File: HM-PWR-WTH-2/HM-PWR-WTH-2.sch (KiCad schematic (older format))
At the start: 42 parts, among them J101 Screw_Terminal_01x02, J102 Conn_01x02_Male, J103 Conn_01x02_Male, J104 Conn_01x02_Male, J105 Conn_01x02_Male, J106 USB_B_Micro, SW101 SW_Push, SW102 SW_Push, U101 LT8606xMSE

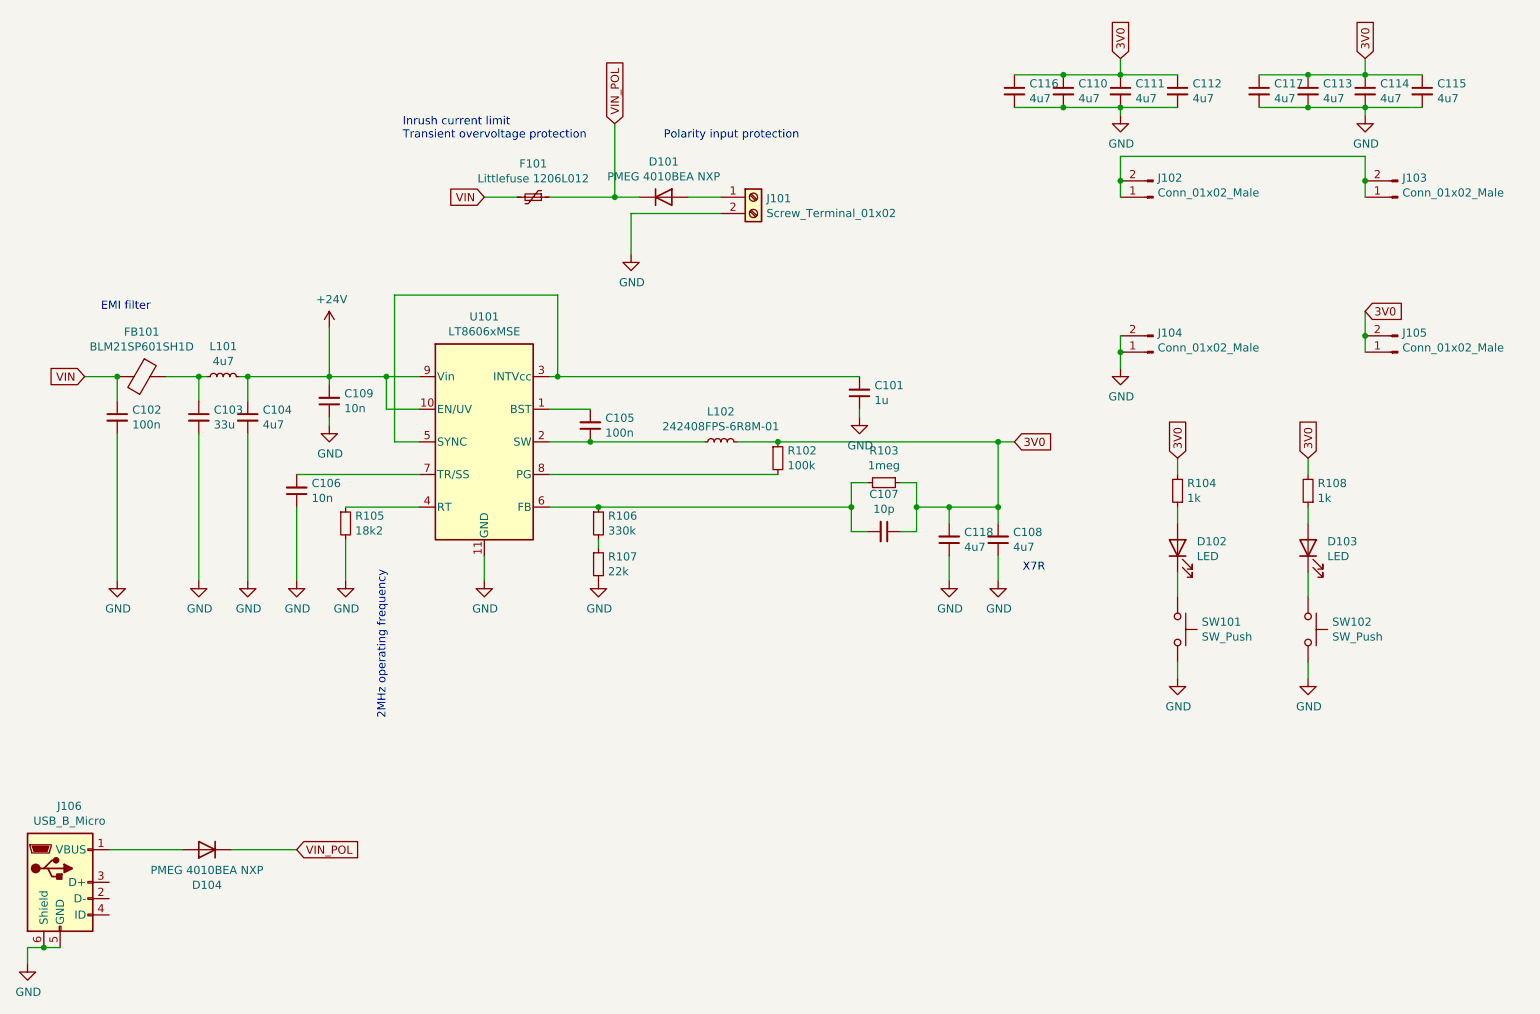
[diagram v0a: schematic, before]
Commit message: HM-PWR-WTH-2: Switch to TPS70930
Signed-off-by: Patrick Rudolph <patrick.rudolph@9elements.com>
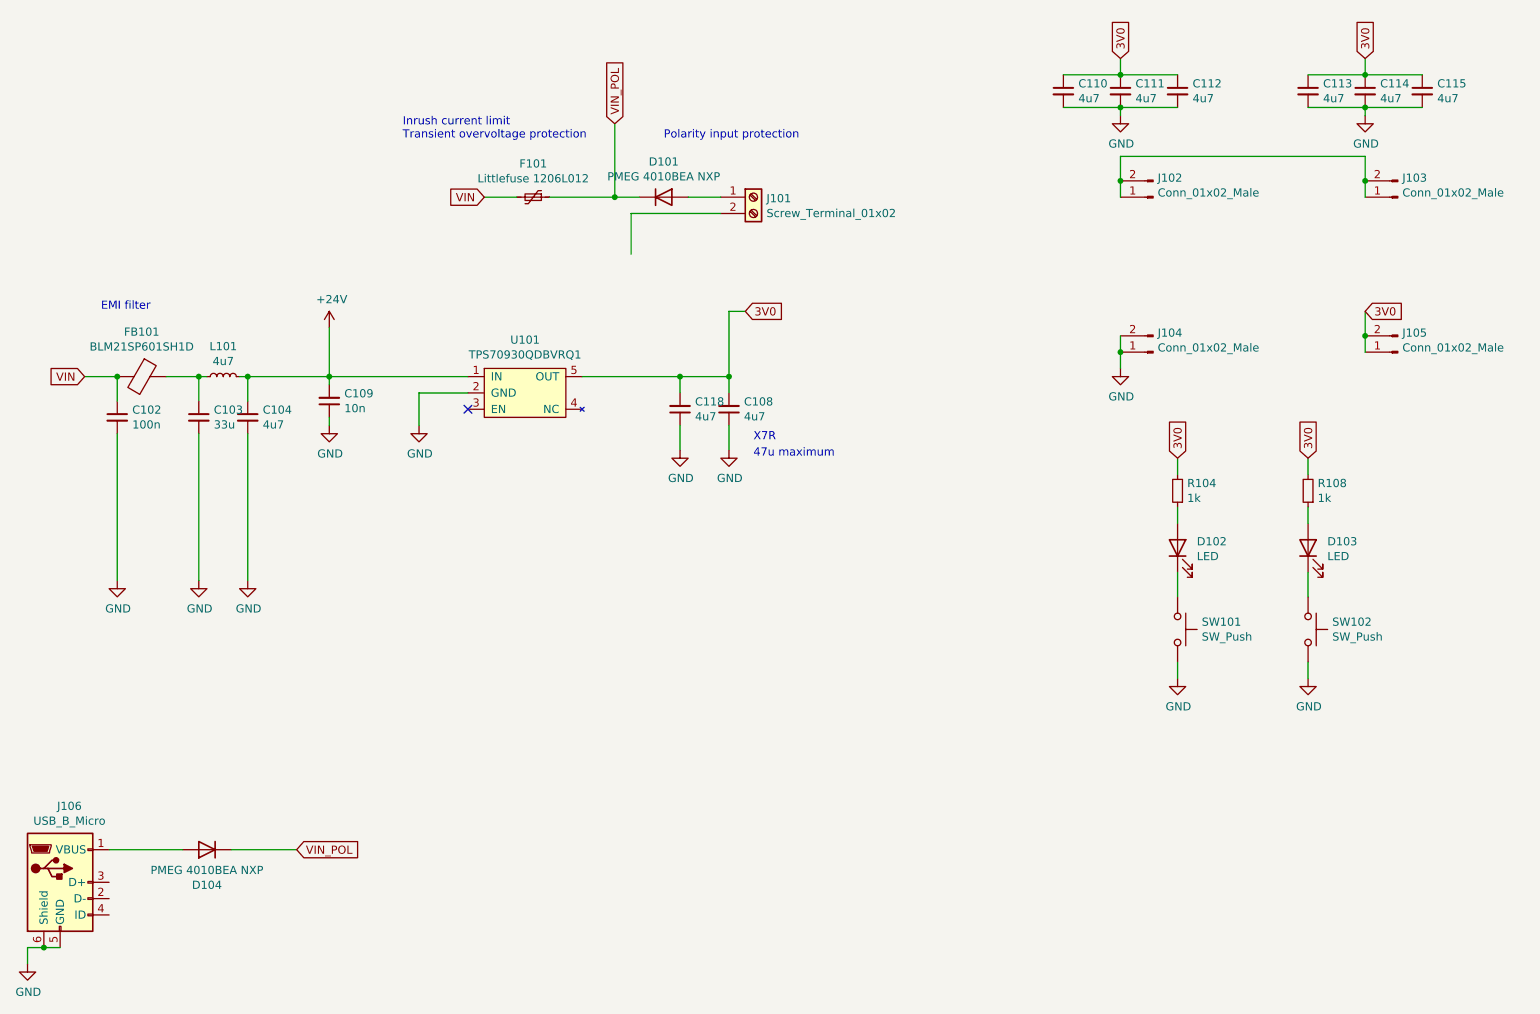
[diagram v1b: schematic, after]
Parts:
- removed C101: 1u, Capacitor_SMD:C_0805_2012Metric_Pad1.18x1.45mm_HandSolder, symbol Device:C_Small
- removed C105: 100n, Capacitor_SMD:C_0603_1608Metric_Pad1.08x0.95mm_HandSolder, symbol Device:C_Small
- removed C106: 10n, Capacitor_SMD:C_0603_1608Metric_Pad1.08x0.95mm_HandSolder, symbol Device:C_Small
- removed C107: 10p, Capacitor_SMD:C_0603_1608Metric_Pad1.08x0.95mm_HandSolder, symbol Device:C_Small
- removed C116, C117: 4u7, Capacitor_SMD:C_1206_3216Metric_Pad1.33x1.80mm_HandSolder, symbol Device:C_Small
- removed L102: 242408FPS-6R8M-01, Inductor_SMD:L_Bourns-SRN6028, symbol Device:L_Small
- removed R102: 100k, Resistor_SMD:R_0603_1608Metric_Pad0.98x0.95mm_HandSolder, symbol Device:R_Small
- removed R103: 1meg, Resistor_SMD:R_0805_2012Metric_Pad1.20x1.40mm_HandSolder, symbol Device:R_Small
- removed R105: 18k2, Resistor_SMD:R_0603_1608Metric_Pad0.98x0.95mm_HandSolder, symbol Device:R_Small
- removed R106: 330k, Resistor_SMD:R_0603_1608Metric_Pad0.98x0.95mm_HandSolder, symbol Device:R_Small
- removed R107: 22k, Resistor_SMD:R_0603_1608Metric_Pad0.98x0.95mm_HandSolder, symbol Device:R_Small
- removed U101: LT8606xMSE, Package_SO:MSOP-10-1EP_3x3mm_P0.5mm_EP1.68x1.88mm, symbol Linear_Technology:LT8606xMSE
- added U101: TPS70930QDBVRQ1, Package_TO_SOT_SMD:SOT-23-5_HandSoldering, symbol TI:TPS709
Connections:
- net +24V: now also U101.1 (IN)
- net 3V0: now also U101.5 (OUT)
- net GND: now also U101.2 (GND); no longer J101.2 (Pin_2)
- no-connect marks 0 -> 1
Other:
- note added: "47u maximum"
- note removed: "2MHz operating frequency"
- moved on the sheet: C108, C118

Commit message: Redesign board
- Replace regulator with one easier to get in germany
- Add LED for minimum current draw of 1mA
- Swap battery + and -

Signed-off-by: Patrick Rudolph <patrick.rudolph@9elements.com>
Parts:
- removed D103: LED, LED_SMD:LED_1206_3216Metric, symbol Device:LED
- removed R108: 1k, Resistor_SMD:R_0805_2012Metric_Pad1.20x1.40mm_HandSolder, symbol Device:R_Small
- removed SW101, SW102: SW_Push, Button_Switch_THT:SW_PUSH_6mm_H5mm, symbol Switch:SW_Push
- removed U101: TPS70930QDBVRQ1, Package_TO_SOT_SMD:SOT-23-5_HandSoldering, symbol TI:TPS709
- added C101: 10p, Capacitor_SMD:C_0603_1608Metric, symbol Device:C_Small
- added R101: 287k, Resistor_SMD:R_0805_2012Metric_Pad1.20x1.40mm_HandSolder, symbol Device:R_Small
- added U101: LT3080xST, Package_TO_SOT_SMD:SOT-223, symbol Regulator_Linear:LT3080xST
- J102, J103, J104, J105: footprint Connector_PinHeader_2.54mm:PinHeader_1x02_P2.54mm_Vertical -> Connector_Wago:Wago_734-132_1x02_P3.50mm_Vertical
- R104: value 1k -> 1k5
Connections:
- net +24V: now also U101.3 (IN)
- net 3V0: now also U101.2 (OUT), U101.4 (OUT)
- net GND: now also D102.1 (K), J101.2 (Pin_2), C101.1, R101.1
- new net: C101.2, R101.2, U101.1 (SET)
- no-connect marks 1 -> 0
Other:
- note added: "1mA @ 1,6V"
- note added: "1mA load for stability"
- note added: "2,87V"
- note added: "2u minimum"
- note added: "Vf=1,4V@1mA"
- note removed: "47u maximum"
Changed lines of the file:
@@
 F 0 "J102" H 8722 1732 50  0000 R CNN
 F 1 "Conn_01x02_Male" H 8722 1823 50  0000 R CNN
-F 2 "Connector_PinHeader_2.54mm:PinHeader_1x02_P2.54mm_Vertical" H 8750 1850 50  0001 C CNN
+F 2 "Connector_Wago:Wago_734-132_1x02_P3.50mm_Vertical" H 8750 1850 50  0001 C CNN
 F 3 "~" H 8750 1850 50  0001 C CNN
 	1    8750 1850
@@
 F 0 "J103" H 10222 1732 50  0000 R CNN
 F 1 "Conn_01x02_Male" H 10222 1823 50  0000 R CNN
-F 2 "Connector_PinHeader_2.54mm:PinHeader_1x02_P2.54mm_Vertical" H 10250 1850 50  0001 C CNN
+F 2 "Connector_Wago:Wago_734-132_1x02_P3.50mm_Vertical" H 10250 1850 50  0001 C CNN
 F 3 "~" H 10250 1850 50  0001 C CNN
 	1    10250 1850
@@
 F 0 "J104" H 8722 2682 50  0000 R CNN
 F 1 "Conn_01x02_Male" H 8722 2773 50  0000 R CNN
-F 2 "Connector_PinHeader_2.54mm:PinHeader_1x02_P2.54mm_Vertical" H 8750 2800 50  0001 C CNN
+F 2 "Connector_Wago:Wago_734-132_1x02_P3.50mm_Vertical" H 8750 2800 50  0001 C CNN
 F 3 "~" H 8750 2800 50  0001 C CNN
 	1    8750 2800
@@
 F 0 "J105" H 10222 2682 50  0000 R CNN
 F 1 "Conn_01x02_Male" H 10222 2773 50  0000 R CNN
-F 2 "Connector_PinHeader_2.54mm:PinHeader_1x02_P2.54mm_Vertical" H 10250 2800 50  0001 C CNN
+F 2 "Connector_Wago:Wago_734-132_1x02_P3.50mm_Vertical" H 10250 2800 50  0001 C CNN
 F 3 "~" H 10250 2800 50  0001 C CNN
 	1    10250 2800
@@
 $EndComp
 $Comp
-L Switch:SW_Push SW101
-U 1 1 606B0668
-P 8900 4500
-F 0 "SW101" V 8854 4648 50  0000 L CNN
-F 1 "SW_Push" V 8945 4648 50  0000 L CNN
-F 2 "Button_Switch_THT:SW_PUSH_6mm_H5mm" H 8900 4700 50  0001 C CNN
-F 3 "~" H 8900 4700 50  0001 C CNN
-	1    8900 4500
-	0    1    1    0
-$EndComp
-$Comp
 L power:GND #PWR0112
 U 1 1 606B110A
@@
 P 8900 3650
 F 0 "R104" H 8841 3604 50  0000 R CNN
-F 1 "1k" H 8841 3695 50  0000 R CNN
+F 1 "1k5" H 8841 3695 50  0000 R CNN
 F 2 "Resistor_SMD:R_0805_2012Metric_Pad1.20x1.40mm_HandSolder" H 8900 3650 50  0001 C CNN
 F 3 "~" H 8900 3650 50  0001 C CNN
@@
 Wire Wire Line
 	8900 3750 8900 3850
-Wire Wire Line
-	8900 4150 8900 4300
-Wire Wire Line
-	8900 4700 8900 4800
 $Comp
 L power:+24V #PWR0113
@@
 Wire Wire Line
 	3700 2950 3200 2950
-$Comp
-L Device:LED D103
-U 1 1 606E14F1
-P 9700 4000
-F 0 "D103" V 9739 3882 50  0000 R CNN
-F 1 "LED" V 9648 3882 50  0000 R CNN
-F 2 "LED_SMD:LED_1206_3216Metric" H 9700 4000 50  0001 C CNN
-F 3 "~" H 9700 4000 50  0001 C CNN
-	1    9700 4000
-	0    -1   -1   0
-$EndComp
-$Comp
-L Switch:SW_Push SW102
-U 1 1 606E14F7
-P 9700 4500
-F 0 "SW102" V 9654 4648 50  0000 L CNN
-F 1 "SW_Push" V 9745 4648 50  0000 L CNN
-F 2 "Button_Switch_THT:SW_PUSH_6mm_H5mm" H 9700 4700 50  0001 C CNN
-F 3 "~" H 9700 4700 50  0001 C CNN
-	1    9700 4500
-	0    1    1    0
-$EndComp
-$Comp
-L power:GND #PWR0114
-U 1 1 606E14FD
-P 9700 4800
-F 0 "#PWR0114" H 9700 4550 50  0001 C CNN
-F 1 "GND" H 9705 4627 50  0000 C CNN
-F 2 "" H 9700 4800 50  0001 C CNN
-F 3 "" H 9700 4800 50  0001 C CNN
-	1    9700 4800
-	1    0    0    -1
-$EndComp
-$Comp
-L Device:R_Small R108
-U 1 1 606E1503
-P 9700 3650
-F 0 "R108" H 9641 3604 50  0000 R CNN
-F 1 "1k" H 9641 3695 50  0000 R CNN
-F 2 "Resistor_SMD:R_0805_2012Metric_Pad1.20x1.40mm_HandSolder" H 9700 3650 50  0001 C CNN
-F 3 "~" H 9700 3650 50  0001 C CNN
-	1    9700 3650
-	-1   0    0    1
-$EndComp
-Text GLabel 9700 3450 1    50   Input ~ 0
-3V0
-Wire Wire Line
-	9700 3450 9700 3550
-Wire Wire Line
-	9700 3750 9700 3850
-Wire Wire Line
-	9700 4150 9700 4300
-Wire Wire Line
-	9700 4700 9700 4800
 $Comp
 L Device:Polyfuse_Small F101
@@
 	2050 6450 1950 6450
 $Comp
-L TI:TPS709 U101
-U 1 1 60792795
-P 4900 3250
-F 0 "U101" H 4900 3775 50  0000 C CNN
-F 1 "TPS70930QDBVRQ1" H 4900 3684 50  0000 C CNN
-F 2 "Package_TO_SOT_SMD:SOT-23-5_HandSoldering" H 4900 3250 50  0001 C CNN
-F 3 "https://www.ti.com/lit/gpn/tps709" H 4900 3250 50  0001 C CNN
-	1    4900 3250
-	1    0    0    -1
-$EndComp
-$Comp
 L power:GND #PWR0101
 U 1 1 60797D46
-P 4250 3250
-F 0 "#PWR0101" H 4250 3000 50  0001 C CNN
-F 1 "GND" H 4255 3077 50  0000 C CNN
-F 2 "" H 4250 3250 50  0001 C CNN
-F 3 "" H 4250 3250 50  0001 C CNN
-	1    4250 3250
+P 4350 3450
+F 0 "#PWR0101" H 4350 3200 50  0001 C CNN
+F 1 "GND" H 4355 3277 50  0000 C CNN
+F 2 "" H 4350 3450 50  0001 C CNN
+F 3 "" H 4350 3450 50  0001 C CNN
+	1    4350 3450
 	1    0    0    -1
 $EndComp
 Wire Wire Line
 	4550 2950 3700 2950
-Wire Wire Line
-	4250 3250 4250 3050
-Wire Wire Line
-	4250 3050 4550 3050
-Wire Wire Line
-	5250 2950 5850 2950
+Text Notes 6300 3450 0    50   ~ 0
+2u minimum
+$Comp
+L Regulator_Linear:LT3080xST U101
+U 1 1 60982B2E
+P 4950 2950
+F 0 "U101" H 4950 3217 50  0000 C CNN
+F 1 "LT3080xST" H 4950 3126 50  0000 C CNN
+F 2 "Package_TO_SOT_SMD:SOT-223" H 4950 2650 50  0001 C CNN
+F 3 "https://www.analog.com/media/en/technical-documentation/data-sheets/3080fc.pdf" H 3230 3720 50  0001 C CNN
+	1    4950 2950
+	1    0    0    -1
+$EndComp
+$Comp
+L Device:R_Small R101
+U 1 1 60983458
+P 4350 3200
+F 0 "R101" H 4291 3154 50  0000 R CNN
+F 1 "287k" H 4291 3245 50  0000 R CNN
+F 2 "Resistor_SMD:R_0805_2012Metric_Pad1.20x1.40mm_HandSolder" H 4350 3200 50  0001 C CNN
+F 3 "~" H 4350 3200 50  0001 C CNN
+	1    4350 3200
+	-1   0    0    1
+$EndComp
+Wire Wire Line
+	5350 3050 5350 2950
+Wire Wire Line
+	5350 2950 5850 2950
+Connection ~ 5350 2950
 Connection ~ 5850 2950
-NoConn ~ 4550 3150
-Text Notes 6300 3450 0    50   ~ 0
-47u maximum
+$Comp
+L Device:C_Small C101
+U 1 1 609864B0
+P 4000 3200
+F 0 "C101" H 3908 3154 50  0000 R CNN
+F 1 "10p" H 3908 3245 50  0000 R CNN
+F 2 "Capacitor_SMD:C_0603_1608Metric" H 4000 3200 50  0001 C CNN
+F 3 "~" H 4000 3200 50  0001 C CNN
+	1    4000 3200
+	-1   0    0    1
+$EndComp
+Wire Wire Line
+	4000 3100 4350 3100
+Wire Wire Line
+	4350 3100 4350 3050
+Wire Wire Line
+	4350 3050 4550 3050
+Connection ~ 4350 3100
+Wire Wire Line
+	4000 3300 4350 3300
+Wire Wire Line
+	4350 3300 4350 3450
+Connection ~ 4350 3300
+Text Notes 5150 2700 0    50   ~ 0
+1mA load for stability
+$Comp
+L power:GND #PWR0102
+U 1 1 6098F5E5
+P 5550 2200
+F 0 "#PWR0102" H 5550 1950 50  0001 C CNN
+F 1 "GND" H 5555 2027 50  0000 C CNN
+F 2 "" H 5550 2200 50  0001 C CNN
+F 3 "" H 5550 2200 50  0001 C CNN
+	1    5550 2200
+	1    0    0    -1
+$EndComp
+Text Notes 4450 3400 0    50   ~ 0
+2,87V
+Wire Wire Line
+	8900 4150 8900 4800
+Text Notes 9150 4200 0    50   ~ 0
+Vf=1,4V@1mA
+Text Notes 9150 3700 0    50   ~ 0
+1mA @ 1,6V
 $EndSCHEMATC

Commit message: Redesign board
- Move all parts to middle and back
- Use less capacitors
- Add mounting holes
- Add battery symbols

Signed-off-by: Patrick Rudolph <patrick.rudolph@9elements.com>
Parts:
- removed C110, C112, C113, C115: 4u7, Capacitor_SMD:C_1206_3216Metric_Pad1.33x1.80mm_HandSolder, symbol Device:C_Small
- added H101: MountingHole, MountingHole:MountingHole_3.2mm_M3_ISO14580, symbol Mechanical:MountingHole
- added H102: MountingHole, MountingHole:MountingHole_3.2mm_M3, symbol Mechanical:MountingHole
- added J107, J108: Conn_01x01_Male, Connector_Pin:Pin_D1.4mm_L8.5mm_W2.8mm_FlatFork, symbol Connector:Conn_01x01_Male
- C103: value 33u -> 100n; footprint Capacitor_SMD:C_1206_3216Metric_Pad1.33x1.80mm_HandSolder -> Capacitor_SMD:C_0805_2012Metric
- C111, C114: value 4u7 -> 33u; footprint Capacitor_SMD:C_1206_3216Metric_Pad1.33x1.80mm_HandSolder -> Capacitor_SMD:C_1812_4532Metric_Pad1.57x3.40mm_HandSolder
- R101: Tolerance (none) -> 5%
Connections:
- no-connect marks 0 -> 6
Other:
- note added: "X5R"
- note added: "sets 2,87V @ OUT"
- note removed: "2,87V"
- note removed: "X7R"
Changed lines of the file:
@@
 P 2900 3200
 F 0 "C103" H 2992 3246 50  0000 L CNN
-F 1 "33u" H 2992 3155 50  0000 L CNN
-F 2 "Capacitor_SMD:C_1206_3216Metric_Pad1.33x1.80mm_HandSolder" H 2900 3200 50  0001 C CNN
+F 1 "100n" H 2992 3155 50  0000 L CNN
+F 2 "Capacitor_SMD:C_0805_2012Metric" H 2900 3200 50  0001 C CNN
 F 3 "~" H 2900 3200 50  0001 C CNN
 	1    2900 3200
@@
 	2900 2950 2950 2950
 $Comp
-L Device:C_Small C110
-U 1 1 60748F7A
-P 8200 1200
-F 0 "C110" H 8292 1246 50  0000 L CNN
-F 1 "4u7" H 8292 1155 50  0000 L CNN
-F 2 "Capacitor_SMD:C_1206_3216Metric_Pad1.33x1.80mm_HandSolder" H 8200 1200 50  0001 C CNN
-F 3 "~" H 8200 1200 50  0001 C CNN
-	1    8200 1200
-	1    0    0    -1
-$EndComp
-$Comp
 L Device:C_Small C111
 U 1 1 60749C96
 P 8550 1200
 F 0 "C111" H 8642 1246 50  0000 L CNN
-F 1 "4u7" H 8642 1155 50  0000 L CNN
-F 2 "Capacitor_SMD:C_1206_3216Metric_Pad1.33x1.80mm_HandSolder" H 8550 1200 50  0001 C CNN
+F 1 "33u" H 8642 1155 50  0000 L CNN
+F 2 "Capacitor_SMD:C_1812_4532Metric_Pad1.57x3.40mm_HandSolder" H 8550 1200 50  0001 C CNN
 F 3 "~" H 8550 1200 50  0001 C CNN
 	1    8550 1200
-	1    0    0    -1
-$EndComp
-$Comp
-L Device:C_Small C112
-U 1 1 6074A0D1
-P 8900 1200
-F 0 "C112" H 8992 1246 50  0000 L CNN
-F 1 "4u7" H 8992 1155 50  0000 L CNN
-F 2 "Capacitor_SMD:C_1206_3216Metric_Pad1.33x1.80mm_HandSolder" H 8900 1200 50  0001 C CNN
-F 3 "~" H 8900 1200 50  0001 C CNN
-	1    8900 1200
-	1    0    0    -1
-$EndComp
-$Comp
-L Device:C_Small C113
-U 1 1 6074F614
-P 9700 1200
-F 0 "C113" H 9792 1246 50  0000 L CNN
-F 1 "4u7" H 9792 1155 50  0000 L CNN
-F 2 "Capacitor_SMD:C_1206_3216Metric_Pad1.33x1.80mm_HandSolder" H 9700 1200 50  0001 C CNN
-F 3 "~" H 9700 1200 50  0001 C CNN
-	1    9700 1200
 	1    0    0    -1
 $EndComp
@@
 P 10050 1200
 F 0 "C114" H 10142 1246 50  0000 L CNN
-F 1 "4u7" H 10142 1155 50  0000 L CNN
-F 2 "Capacitor_SMD:C_1206_3216Metric_Pad1.33x1.80mm_HandSolder" H 10050 1200 50  0001 C CNN
+F 1 "33u" H 10142 1155 50  0000 L CNN
+F 2 "Capacitor_SMD:C_1812_4532Metric_Pad1.57x3.40mm_HandSolder" H 10050 1200 50  0001 C CNN
 F 3 "~" H 10050 1200 50  0001 C CNN
 	1    10050 1200
 	1    0    0    -1
 $EndComp
-$Comp
-L Device:C_Small C115
-U 1 1 6074F620
-P 10400 1200
-F 0 "C115" H 10492 1246 50  0000 L CNN
-F 1 "4u7" H 10492 1155 50  0000 L CNN
-F 2 "Capacitor_SMD:C_1206_3216Metric_Pad1.33x1.80mm_HandSolder" H 10400 1200 50  0001 C CNN
-F 3 "~" H 10400 1200 50  0001 C CNN
-	1    10400 1200
-	1    0    0    -1
-$EndComp
-Wire Wire Line
-	9700 1100 10050 1100
-Wire Wire Line
-	10050 1100 10400 1100
-Connection ~ 10050 1100
-Wire Wire Line
-	10400 1300 10050 1300
-Wire Wire Line
-	10050 1300 9700 1300
-Connection ~ 10050 1300
-Wire Wire Line
-	8200 1100 8550 1100
-Wire Wire Line
-	8550 1100 8900 1100
-Connection ~ 8550 1100
-Wire Wire Line
-	8900 1300 8550 1300
-Wire Wire Line
-	8550 1300 8200 1300
-Connection ~ 8550 1300
 Wire Wire Line
 	10050 2550 10050 2700
@@
 	8550 1100 8550 1000
 Text Notes 6300 3350 0    50   ~ 0
-X7R
+X5R
 $Comp
 L Device:C_Small C118
@@
 F 2 "Resistor_SMD:R_0805_2012Metric_Pad1.20x1.40mm_HandSolder" H 4350 3200 50  0001 C CNN
 F 3 "~" H 4350 3200 50  0001 C CNN
+F 4 "5%" H 4250 3350 50  0000 C CNN "Tolerance"
 	1    4350 3200
 	-1   0    0    1
@@
 	1    0    0    -1
 $EndComp
-Text Notes 4450 3400 0    50   ~ 0
-2,87V
+Text Notes 4600 3400 0    50   ~ 0
+sets 2,87V  @ OUT
 Wire Wire Line
 	8900 4150 8900 4800
@@
 Text Notes 9150 3700 0    50   ~ 0
 1mA @ 1,6V
+$Comp
+L Mechanical:MountingHole H102
+U 1 1 609B0030
+P 5700 6600
+F 0 "H102" H 5800 6646 50  0000 L CNN
+F 1 "MountingHole" H 5800 6555 50  0000 L CNN
+F 2 "MountingHole:MountingHole_3.2mm_M3" H 5700 6600 50  0001 C CNN
+F 3 "~" H 5700 6600 50  0001 C CNN
+	1    5700 6600
+	1    0    0    -1
+$EndComp
+$Comp
+L Mechanical:MountingHole H101
+U 1 1 609B0960
+P 5700 6350
+F 0 "H101" H 5800 6396 50  0000 L CNN
+F 1 "MountingHole" H 5800 6305 50  0000 L CNN
+F 2 "MountingHole:MountingHole_3.2mm_M3_ISO14580" H 5700 6350 50  0001 C CNN
+F 3 "~" H 5700 6350 50  0001 C CNN
+	1    5700 6350
+	1    0    0    -1
+$EndComp
+NoConn ~ 2350 6050
+NoConn ~ 2350 6150
+NoConn ~ 2350 6250
+$Comp
+L Connector:Conn_01x01_Male J107
+U 1 1 609D9F36
+P 8750 2050
+F 0 "J107" H 8722 1982 50  0000 R CNN
+F 1 "Conn_01x01_Male" H 8722 2073 50  0000 R CNN
+F 2 "Connector_Pin:Pin_D1.4mm_L8.5mm_W2.8mm_FlatFork" H 8750 2050 50  0001 C CNN
+F 3 "~" H 8750 2050 50  0001 C CNN
+	1    8750 2050
+	-1   0    0    1
+$EndComp
+$Comp
+L Connector:Conn_01x01_Male J108
+U 1 1 609DA7D9
+P 8750 2250
+F 0 "J108" H 8722 2182 50  0000 R CNN
+F 1 "Conn_01x01_Male" H 8722 2273 50  0000 R CNN
+F 2 "Connector_Pin:Pin_D1.4mm_L8.5mm_W2.8mm_FlatFork" H 8750 2250 50  0001 C CNN
+F 3 "~" H 8750 2250 50  0001 C CNN
+	1    8750 2250
+	-1   0    0    1
+$EndComp
+NoConn ~ 8550 2050
+NoConn ~ 8550 2250
+NoConn ~ 5700 6400
 $EndSCHEMATC
